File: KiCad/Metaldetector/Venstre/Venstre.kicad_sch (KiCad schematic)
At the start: 16 parts, among them Q1 NMOS_IRL530, Q3 NMOS_IRL530, Q5 NMOS_IRL530

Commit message: ændret kicad opsætning
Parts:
- added C_Load1: 820n, symbol Device:C
- added V_Out1: Conn_01x01_Pin, symbol Connector:Conn_01x01_Pin
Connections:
- net Venstre_out renamed Meas_V_Out
- net Meas_V_Out: now also C_Load1.2
- new net: C_Load1.1, V_Out1.1 (Pin_1)
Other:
- moved on the sheet: 5V_pin1, 9V_pin1, C1, D1, D2, GND_pin1, Meas_V1, PWM_1_In1, PWM_2_NOT_In1, Q1, Q3, Q5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

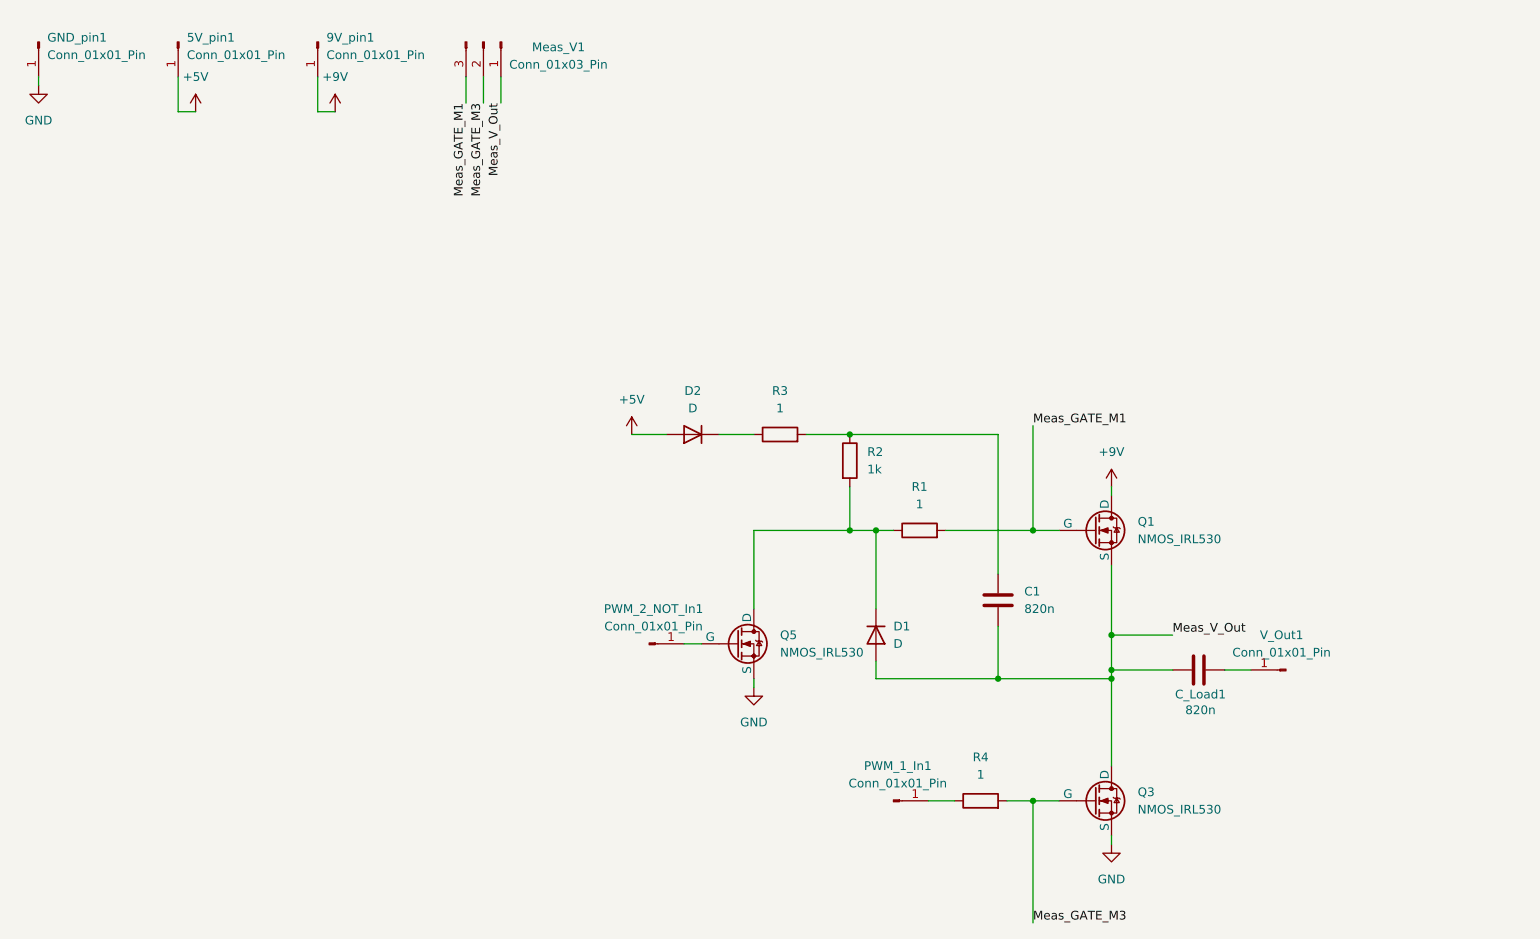
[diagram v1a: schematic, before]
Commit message: nyste pcb design til AP forstærker
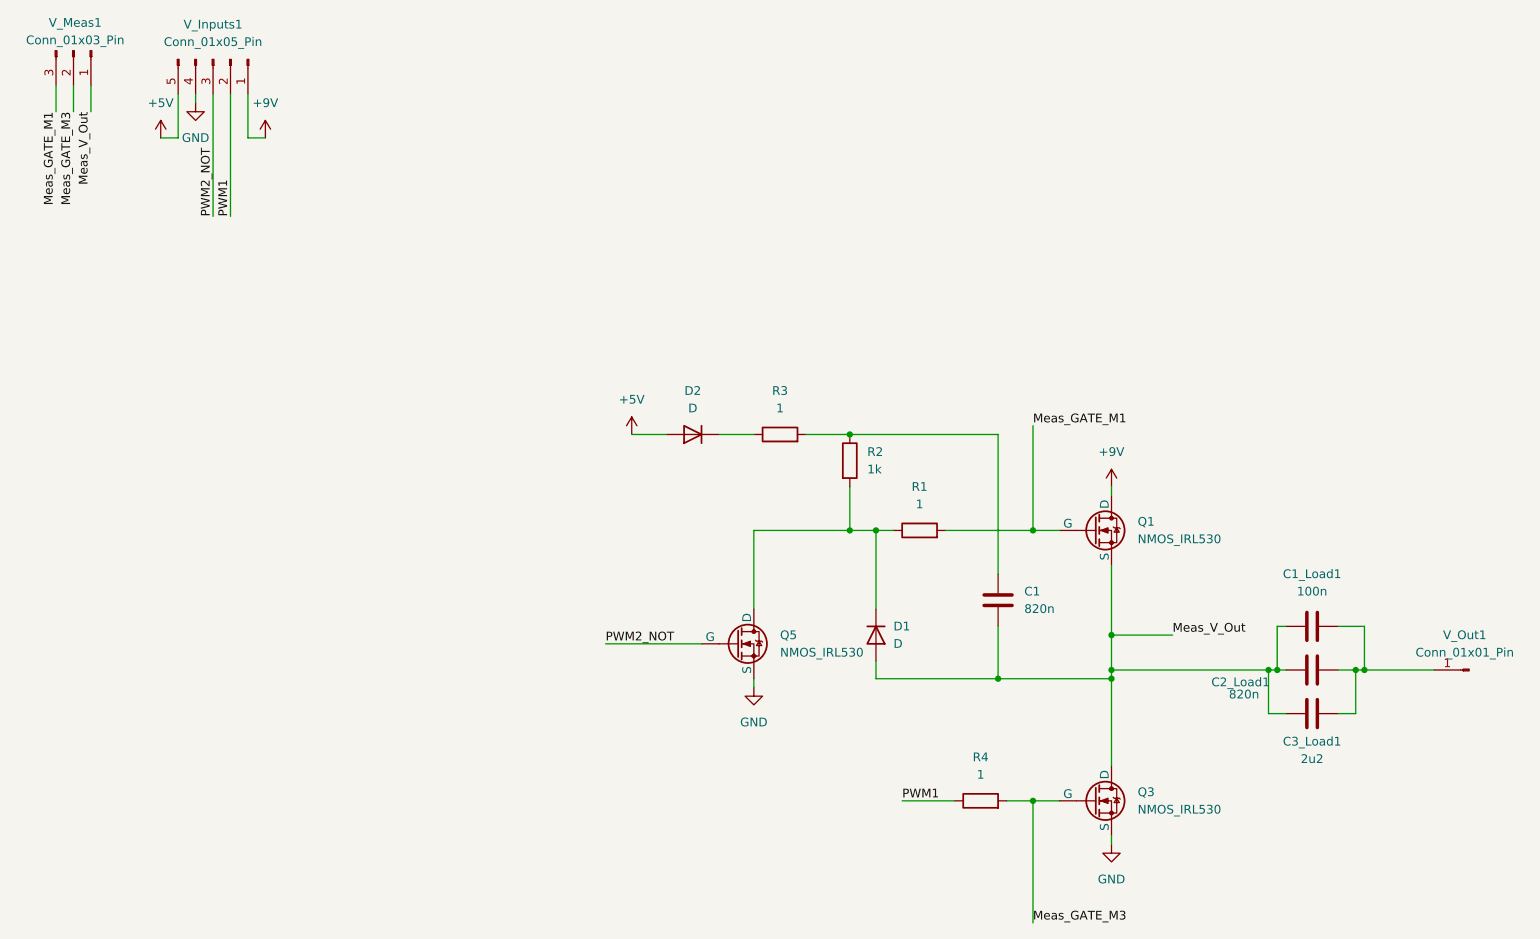
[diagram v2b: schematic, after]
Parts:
- removed 5V_pin1, 9V_pin1, GND_pin1, PWM_1_In1, PWM_2_NOT_In1: Conn_01x01_Pin, symbol Connector:Conn_01x01_Pin
- added C1_Load1: 100n, Capacitor_THT:C_Rect_L9.0mm_W2.5mm_P7.50mm_MKT, symbol Device:C
- added C3_Load1: 2u2, Capacitor_THT:C_Rect_L24.0mm_W7.0mm_P22.50mm_MKT, symbol Device:C
- added V_Inputs1: Conn_01x05_Pin, Connector_PinHeader_2.54mm:PinHeader_1x05_P2.54mm_Horizontal, symbol Connector:Conn_01x05_Pin
- C1: footprint (none) -> Capacitor_THT:C_Rect_L16.5mm_W8.7mm_P15.00mm_MKT
- C2_Load1: renamed from C_Load1; footprint (none) -> Capacitor_THT:C_Rect_L16.5mm_W8.7mm_P15.00mm_MKT
- D1, D2: footprint (none) -> Diode_THT:D_DO-41_SOD81_P2.54mm_Vertical_AnodeUp
- Q1, Q3, Q5: footprint (none) -> Package_TO_SOT_THT:TO-220-3_Vertical
- R1, R2, R3, R4: footprint (none) -> Resistor_THT:R_Axial_DIN0204_L3.6mm_D1.6mm_P5.08mm_Horizontal
- V_Meas1: renamed from Meas_V1; footprint (none) -> Connector_PinHeader_2.54mm:PinHeader_1x03_P2.54mm_Vertical
- V_Out1: footprint (none) -> Connector_PinHeader_2.54mm:PinHeader_1x01_P2.54mm_Vertical
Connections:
- net +5V: now also V_Inputs1.5 (Pin_5)
- net +9V: now also V_Inputs1.1 (Pin_1)
- net GND: now also V_Inputs1.4 (Pin_4)
- net Meas_V_Out: now also C1_Load1.1, C3_Load1.1
- net PWM1: now reaches R4.1
- net PWM1: now also V_Inputs1.2 (Pin_2)
- net at C2_Load1.1, V_Out1.1 (Pin_1): now also C1_Load1.2, C3_Load1.2
- net PWM2_NOT: now reaches Q5.2 (G)
- net PWM2_NOT: now also V_Inputs1.3 (Pin_3)
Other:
- moved on the sheet: C2_Load1, V_Meas1, V_Out1
